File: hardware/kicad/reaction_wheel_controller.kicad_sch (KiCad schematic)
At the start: 0 parts

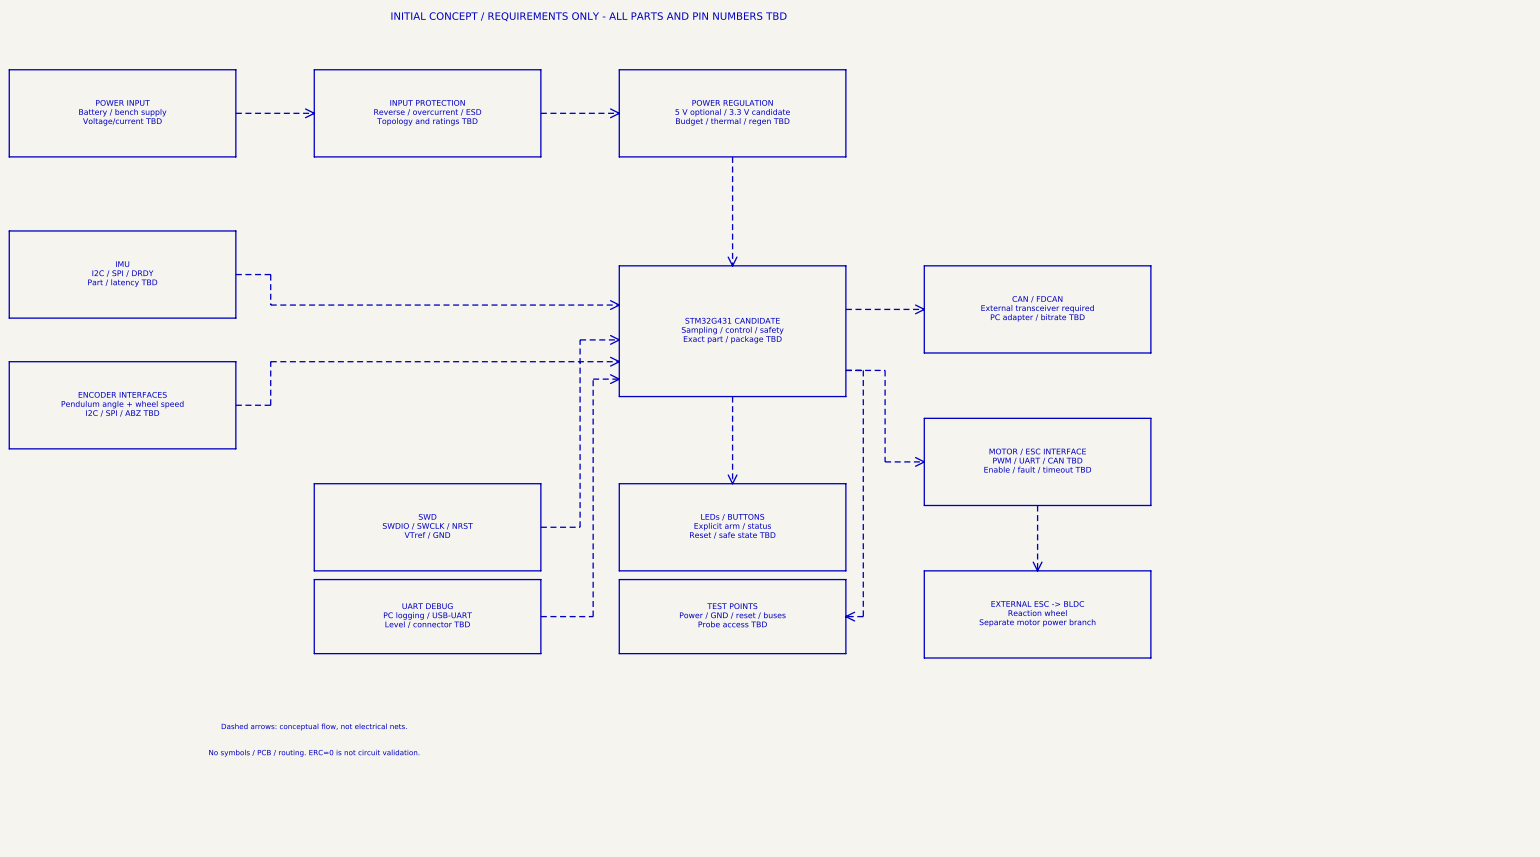
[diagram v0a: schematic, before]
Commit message: hardware: add verified STM32G431 power and SWD circuit
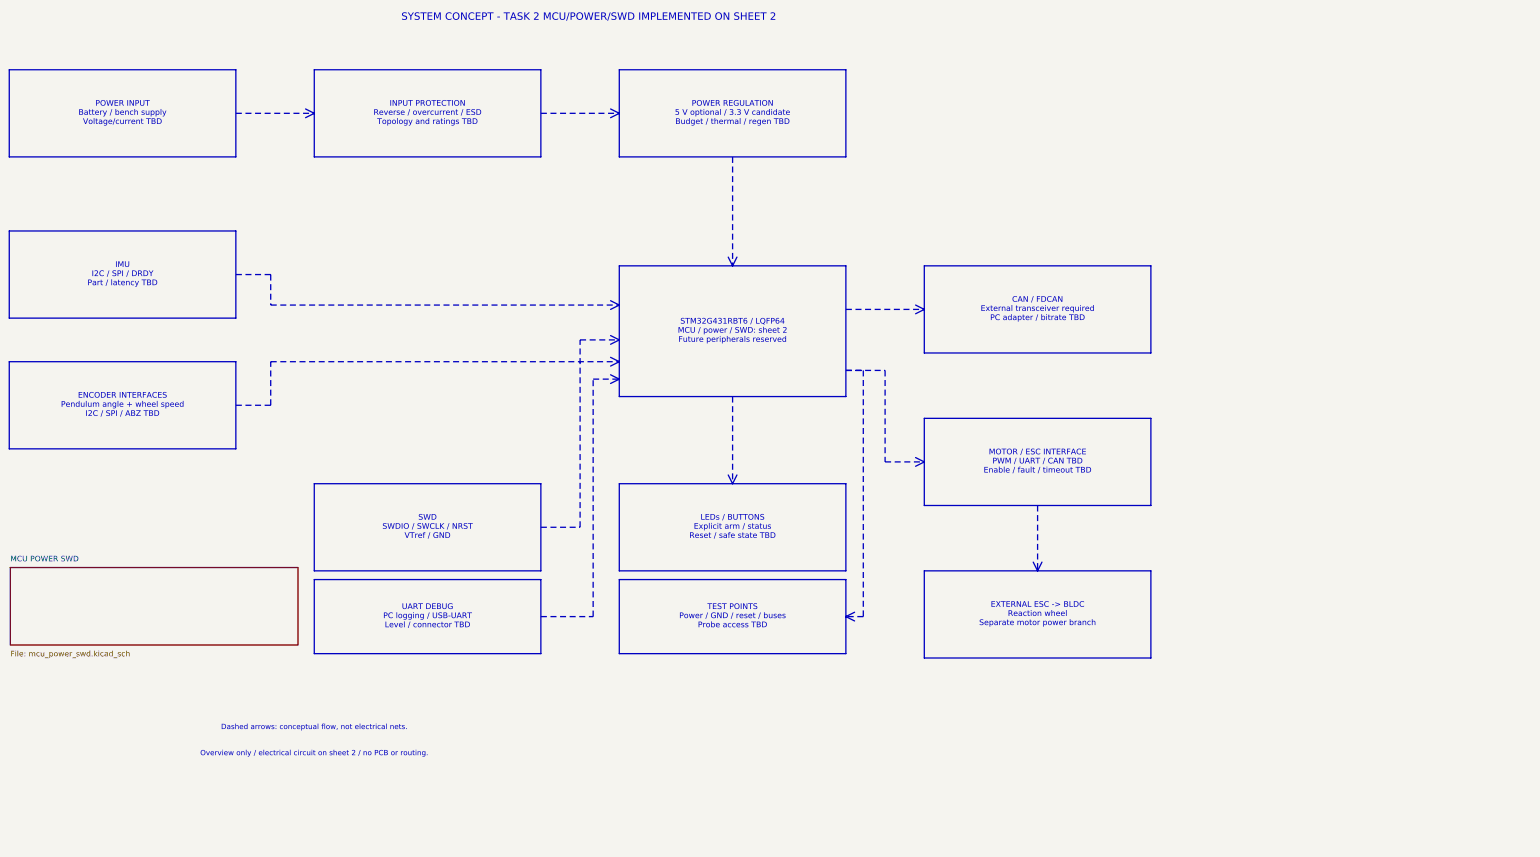
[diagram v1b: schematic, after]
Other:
- added sheet MCU POWER SWD (mcu_power_swd.kicad_sch)
- note added: "Overview only / electrical circuit on sheet 2 / no PCB or routing."
- note added: "STM32G431RBT6 / LQFP64 MCU / power / SWD: sheet 2 Future peripherals reserved"
- note added: "SYSTEM CONCEPT - TASK 2 MCU/POWER/SWD IMPLEMENTED ON SHEET 2"
- note removed: "INITIAL CONCEPT / REQUIREMENTS ONLY - ALL PARTS AND PIN NUMBERS TBD"
- note removed: "No symbols / PCB / routing. ERC=0 is not circuit validation."
- note removed: "STM32G431 CANDIDATE Sampling / control / safety Exact part / package TBD"
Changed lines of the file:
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@@
     (date "2026-10-02")
     (rev "0.1-concept")
-    (comment 1 "No components or electrical nets; not a finished circuit")
+    (comment 1 "Overview blocks only; electrical implementation on MCU POWER SWD sheet")
   )
-  (text "INITIAL CONCEPT / REQUIREMENTS ONLY - ALL PARTS AND PIN NUMBERS TBD" (at 148 16 0)
+  (text "SYSTEM CONCEPT - TASK 2 MCU/POWER/SWD IMPLEMENTED ON SHEET 2" (at 148 16 0)
     (effects (font (size 1.7 1.7))))
   (rectangle (start 15 28) (end 67 48)
@@
   (rectangle (start 155 73) (end 207 103)
     (stroke (width 0.254) (type default)) (fill (type none)))
-  (text "STM32G431 CANDIDATE\nSampling / control / safety\nExact part / package TBD" (at 181.0 88.0 0)
+  (text "STM32G431RBT6 / LQFP64\nMCU / power / SWD: sheet 2\nFuture peripherals reserved" (at 181.0 88.0 0)
     (effects (font (size 1.3 1.3))))
   (polyline (pts (xy 181 48) (xy 181 73)) (stroke (width 0.254) (type dash))
@@
   (text "Dashed arrows: conceptual flow, not electrical nets." (at 85 179 0)
     (effects (font (size 1.2 1.2))))
-  (text "No symbols / PCB / routing. ERC=0 is not circuit validation." (at 85 185 0)
+  (text "Overview only / electrical circuit on sheet 2 / no PCB or routing." (at 85 185 0)
     (effects (font (size 1.2 1.2))))
   (sheet_instances (path "/" (page "1")))
+(sheet (at 15.24 142.24) (size 66.04 17.78) (stroke (width 0.254) (type default)) (fill (color 0 0 0 0)) (property "Sheetname" "MCU POWER SWD" (at 15.24 140.97 0) (effects (font (size 1.27 1.27)) (justify left bottom))) (property "Sheetfile" "mcu_power_swd.kicad_sch" (at 15.24 161.29 0) (effects (font (size 1.27 1.27)) (justify left top))) (instances (project "reaction_wheel_controller" (path "/56c7795e-d739-4c45-a73e-6c5ecdfd94b9" (page "2")))))
 )

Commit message: hardware: add verified CAN sensor and ESC interfaces
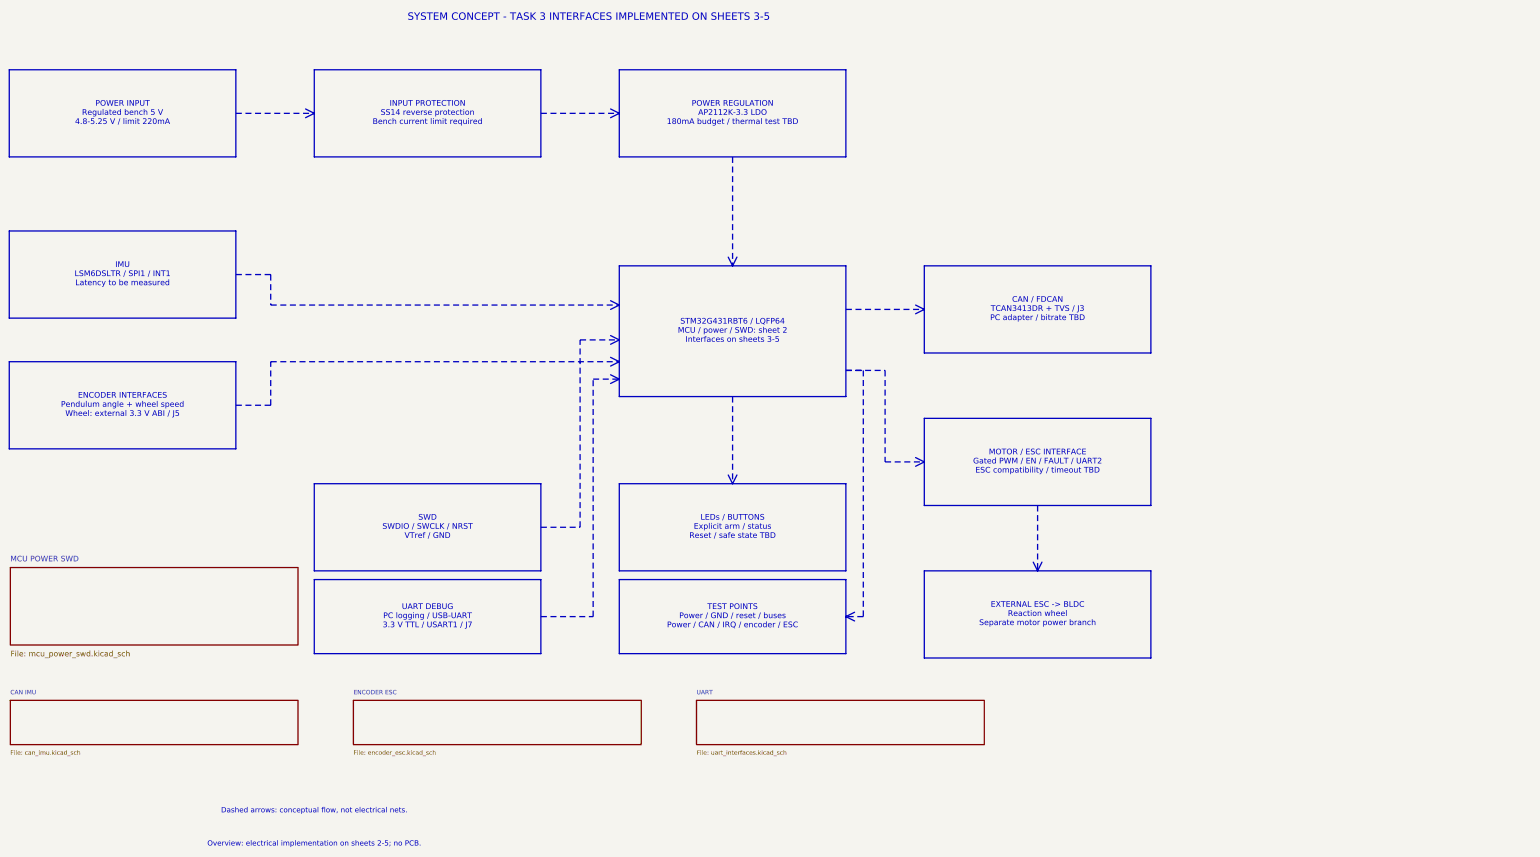
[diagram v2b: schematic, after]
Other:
- added sheet CAN IMU (can_imu.kicad_sch)
- added sheet ENCODER ESC (encoder_esc.kicad_sch)
- added sheet UART (uart_interfaces.kicad_sch)
- note added: "CAN / FDCAN TCAN3413DR + TVS / J3 PC adapter / bitrate TBD"
- note added: "ENCODER INTERFACES Pendulum angle + wheel speed Wheel: external 3.3 V ABI / J5"
- note added: "IMU LSM6DSLTR / SPI1 / INT1 Latency to be measured"
- note added: "INPUT PROTECTION SS14 reverse protection Bench current limit required"
- note added: "MOTOR / ESC INTERFACE Gated PWM / EN / FAULT / UART2 ESC compatibility / timeout TBD"
- note added: "Overview: electrical implementation on sheets 2-5; no PCB."
- note added: "POWER INPUT Regulated bench 5 V 4.8-5.25 V / limit 220mA"
- note added: "POWER REGULATION AP2112K-3.3 LDO 180mA budget / thermal test TBD"
- note added: "STM32G431RBT6 / LQFP64 MCU / power / SWD: sheet 2 Interfaces on sheets 3-5"
- note added: "SYSTEM CONCEPT - TASK 3 INTERFACES IMPLEMENTED ON SHEETS 3-5"
- note added: "TEST POINTS Power / GND / reset / buses Power / CAN / IRQ / encoder / ESC"
- note added: "UART DEBUG PC logging / USB-UART 3.3 V TTL / USART1 / J7"
- note removed: "CAN / FDCAN External transceiver required PC adapter / bitrate TBD"
- note removed: "ENCODER INTERFACES Pendulum angle + wheel speed I2C / SPI / ABZ TBD"
- note removed: "IMU I2C / SPI / DRDY Part / latency TBD"
- note removed: "INPUT PROTECTION Reverse / overcurrent / ESD Topology and ratings TBD"
- note removed: "MOTOR / ESC INTERFACE PWM / UART / CAN TBD Enable / fault / timeout TBD"
- note removed: "Overview only / electrical circuit on sheet 2 / no PCB or routing."
- note removed: "POWER INPUT Battery / bench supply Voltage/current TBD"
- note removed: "POWER REGULATION 5 V optional / 3.3 V candidate Budget / thermal / regen TBD"
- note removed: "STM32G431RBT6 / LQFP64 MCU / power / SWD: sheet 2 Future peripherals reserved"
- note removed: "SYSTEM CONCEPT - TASK 2 MCU/POWER/SWD IMPLEMENTED ON SHEET 2"
- note removed: "TEST POINTS Power / GND / reset / buses Probe access TBD"
- note removed: "UART DEBUG PC logging / USB-UART Level / connector TBD"
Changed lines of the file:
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@@
   (generator "reaction-wheel-pendulum")
   (generator_version "0.1")
-  (paper "A4")
+  (paper "A3")
   (title_block
     (title "Reaction Wheel Controller - Concept Blocks")
     (date "2026-10-02")
-    (rev "0.1-concept")
-    (comment 1 "Overview blocks only; electrical implementation on MCU POWER SWD sheet")
+    (rev "0.3")
+    (comment 1 "Overview blocks only; electrical implementation on sheets 2-5")
   )
-  (text "SYSTEM CONCEPT - TASK 2 MCU/POWER/SWD IMPLEMENTED ON SHEET 2" (at 148 16 0)
+  (text "SYSTEM CONCEPT - TASK 3 INTERFACES IMPLEMENTED ON SHEETS 3-5" (at 148 16 0)
     (effects (font (size 1.7 1.7))))
   (rectangle (start 15 28) (end 67 48)
     (stroke (width 0.254) (type default)) (fill (type none)))
-  (text "POWER INPUT\nBattery / bench supply\nVoltage/current TBD" (at 41.0 38.0 0)
+  (text "POWER INPUT\nRegulated bench 5 V\n4.8-5.25 V / limit 220mA" (at 41.0 38.0 0)
     (effects (font (size 1.3 1.3))))
   (rectangle (start 85 28) (end 137 48)
     (stroke (width 0.254) (type default)) (fill (type none)))
-  (text "INPUT PROTECTION\nReverse / overcurrent / ESD\nTopology and ratings TBD" (at 111.0 38.0 0)
+  (text "INPUT PROTECTION\nSS14 reverse protection\nBench current limit required" (at 111.0 38.0 0)
     (effects (font (size 1.3 1.3))))
   (rectangle (start 155 28) (end 207 48)
     (stroke (width 0.254) (type default)) (fill (type none)))
-  (text "POWER REGULATION\n5 V optional / 3.3 V candidate\nBudget / thermal / regen TBD" (at 181.0 38.0 0)
+  (text "POWER REGULATION\nAP2112K-3.3 LDO\n180mA budget / thermal test TBD" (at 181.0 38.0 0)
     (effects (font (size 1.3 1.3))))
   (polyline (pts (xy 67 38) (xy 85 38)) (stroke (width 0.254) (type dash))
@@
   (rectangle (start 155 73) (end 207 103)
     (stroke (width 0.254) (type default)) (fill (type none)))
-  (text "STM32G431RBT6 / LQFP64\nMCU / power / SWD: sheet 2\nFuture peripherals reserved" (at 181.0 88.0 0)
+  (text "STM32G431RBT6 / LQFP64\nMCU / power / SWD: sheet 2\nInterfaces on sheets 3-5" (at 181.0 88.0 0)
     (effects (font (size 1.3 1.3))))
   (polyline (pts (xy 181 48) (xy 181 73)) (stroke (width 0.254) (type dash))
@@
   (rectangle (start 15 65) (end 67 85)
     (stroke (width 0.254) (type default)) (fill (type none)))
-  (text "IMU\nI2C / SPI / DRDY\nPart / latency TBD" (at 41.0 75.0 0)
+  (text "IMU\nLSM6DSLTR / SPI1 / INT1\nLatency to be measured" (at 41.0 75.0 0)
     (effects (font (size 1.3 1.3))))
   (rectangle (start 15 95) (end 67 115)
     (stroke (width 0.254) (type default)) (fill (type none)))
-  (text "ENCODER INTERFACES\nPendulum angle + wheel speed\nI2C / SPI / ABZ TBD" (at 41.0 105.0 0)
+  (text "ENCODER INTERFACES\nPendulum angle + wheel speed\nWheel: external 3.3 V ABI / J5" (at 41.0 105.0 0)
     (effects (font (size 1.3 1.3))))
   (polyline (pts (xy 67 75) (xy 75 75) (xy 75 82) (xy 155 82)) (stroke (width 0.254) (type dash))
@@
   (rectangle (start 225 73) (end 277 93)
     (stroke (width 0.254) (type default)) (fill (type none)))
-  (text "CAN / FDCAN\nExternal transceiver required\nPC adapter / bitrate TBD" (at 251.0 83.0 0)
+  (text "CAN / FDCAN\nTCAN3413DR + TVS / J3\nPC adapter / bitrate TBD" (at 251.0 83.0 0)
     (effects (font (size 1.3 1.3))))
   (polyline (pts (xy 207 83) (xy 225 83)) (stroke (width 0.254) (type dash))
@@
   (rectangle (start 225 108) (end 277 128)
     (stroke (width 0.254) (type default)) (fill (type none)))
-  (text "MOTOR / ESC INTERFACE\nPWM / UART / CAN TBD\nEnable / fault / timeout TBD" (at 251.0 118.0 0)
+  (text "MOTOR / ESC INTERFACE\nGated PWM / EN / FAULT / UART2\nESC compatibility / timeout TBD" (at 251.0 118.0 0)
     (effects (font (size 1.3 1.3))))
   (polyline (pts (xy 207 97) (xy 216 97) (xy 216 118) (xy 225 118)) (stroke (width 0.254) (type dash))
@@
   (rectangle (start 85 145) (end 137 162)
     (stroke (width 0.254) (type default)) (fill (type none)))
-  (text "UART DEBUG\nPC logging / USB-UART\nLevel / connector TBD" (at 111.0 153.5 0)
+  (text "UART DEBUG\nPC logging / USB-UART\n3.3 V TTL / USART1 / J7" (at 111.0 153.5 0)
     (effects (font (size 1.3 1.3))))
   (polyline (pts (xy 137 133) (xy 146 133) (xy 146 90) (xy 155 90)) (stroke (width 0.254) (type dash))
@@
   (rectangle (start 155 145) (end 207 162)
     (stroke (width 0.254) (type default)) (fill (type none)))
-  (text "TEST POINTS\nPower / GND / reset / buses\nProbe access TBD" (at 181.0 153.5 0)
+  (text "TEST POINTS\nPower / GND / reset / buses\nPower / CAN / IRQ / encoder / ESC" (at 181.0 153.5 0)
     (effects (font (size 1.3 1.3))))
   (polyline (pts (xy 181 103) (xy 181 123)) (stroke (width 0.254) (type dash))
@@
   (polyline (pts (xy 209 152.5) (xy 207 153.5) (xy 209 154.5)) (stroke (width 0.254) (type default))
     (fill (type none)))
-  (text "Dashed arrows: conceptual flow, not electrical nets." (at 85 179 0)
+  (text "Dashed arrows: conceptual flow, not electrical nets." (at 85 198.12 0)
     (effects (font (size 1.2 1.2))))
-  (text "Overview only / electrical circuit on sheet 2 / no PCB or routing." (at 85 185 0)
+  (text "Overview: electrical implementation on sheets 2-5; no PCB." (at 85 205.74 0)
     (effects (font (size 1.2 1.2))))
   (sheet_instances (path "/" (page "1")))
 (sheet (at 15.24 142.24) (size 66.04 17.78) (stroke (width 0.254) (type default)) (fill (color 0 0 0 0)) (property "Sheetname" "MCU POWER SWD" (at 15.24 140.97 0) (effects (font (size 1.27 1.27)) (justify left bottom))) (property "Sheetfile" "mcu_power_swd.kicad_sch" (at 15.24 161.29 0) (effects (font (size 1.27 1.27)) (justify left top))) (instances (project "reaction_wheel_controller" (path "/56c7795e-d739-4c45-a73e-6c5ecdfd94b9" (page "2")))))
+(sheet (at 15.24 172.72) (size 66.04 10.16) (stroke (width 0.254) (type default)) (fill (color 0 0 0 0)) (property "Sheetname" "CAN IMU" (at 15.24 171.45 0) (effects (font (size 1 1)) (justify left bottom))) (property "Sheetfile" "can_imu.kicad_sch" (at 15.24 184.15 0) (effects (font (size 1 1)) (justify left top))) (instances (project "reaction_wheel_controller" (path "/56c7795e-d739-4c45-a73e-6c5ecdfd94b9" (page "3")))))
+(sheet (at 93.98 172.72) (size 66.04 10.16) (stroke (width 0.254) (type default)) (fill (color 0 0 0 0)) (property "Sheetname" "ENCODER ESC" (at 93.98 171.45 0) (effects (font (size 1 1)) (justify left bottom))) (property "Sheetfile" "encoder_esc.kicad_sch" (at 93.98 184.15 0) (effects (font (size 1 1)) (justify left top))) (instances (project "reaction_wheel_controller" (path "/56c7795e-d739-4c45-a73e-6c5ecdfd94b9" (page "4")))))
+(sheet (at 172.72 172.72) (size 66.04 10.16) (stroke (width 0.254) (type default)) (fill (color 0 0 0 0)) (property "Sheetname" "UART" (at 172.72 171.45 0) (effects (font (size 1 1)) (justify left bottom))) (property "Sheetfile" "uart_interfaces.kicad_sch" (at 172.72 184.15 0) (effects (font (size 1 1)) (justify left top))) (instances (project "reaction_wheel_controller" (path "/56c7795e-d739-4c45-a73e-6c5ecdfd94b9" (page "5")))))
 )
